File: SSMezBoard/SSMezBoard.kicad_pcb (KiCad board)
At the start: 2 copper layers, 2 parts, among them U1 DFRobot_DC_Controller

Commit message: Sort of ready for JLCPCB
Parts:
- removed U1: DFRobot_DC_Controller, PBFootPrintLibrary:DFRobot_DC_Controller
- added J1: Conn_02x10_Odd_Even, Connector_PinHeader_2.54mm:PinHeader_2x10_P2.54mm_Horizontal, F.Cu at (162.9, 75.8)
- added LED1: LED, LED_THT:LED_D5.0mm, F.Cu at (160.1, 108.5)
- added LED2: LED, LED_THT:LED_D5.0mm, F.Cu at (166.1, 64.4)
- added SW1: TACT_SW, Button_Switch_THT:SW_PUSH_6mm, F.Cu at (144.2, 112.7)
- moved A1 40.3 mm to (157.6, 97.6), turned to 180 degrees
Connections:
- net Net-(A1-GND-Pad29) renamed GND
- A1 pad 1: unconnected-(A1-D1/TX-Pad1) -> Net-(A1-D1/TX)
- A1 pad 10: unconnected-(A1-D7-Pad10) -> RIGHT_ENC_B
- A1 pad 11: unconnected-(A1-D8-Pad11) -> LEFT_ENC_A
- A1 pad 12: unconnected-(A1-D9-Pad12) -> LEFT_ENC_B
- A1 pad 13: unconnected-(A1-D10/CS-Pad13) -> SENSOR_LED
- A1 pad 14: unconnected-(A1-D11/COPI-Pad14) -> GPIO_DIAG
- A1 pad 15: unconnected-(A1-D12/CIPO-Pad15) -> GPIO_FRONT
- A1 pad 16: unconnected-(A1-D13/SCK-Pad16) -> Net-(A1-D13/SCK)
- A1 pad 17: Net-(A1-3V3) -> Vcc
- A1 pad 19: unconnected-(A1-A0-Pad19) -> RIGHT_DIAG_ADC
- A1 pad 2: unconnected-(A1-D0/RX-Pad2) -> Net-(A1-D0/RX)
- A1 pad 20: unconnected-(A1-A1-Pad20) -> RIGHT_FRONT_ADC
- A1 pad 21: unconnected-(A1-A2-Pad21) -> LEFT_FRONT_ADC
- A1 pad 22: unconnected-(A1-A3-Pad22) -> LEFT_DIAG_ADC
- A1 pad 23: unconnected-(A1-SDA/A4-Pad23) -> GPIO12_D18
- A1 pad 30: unconnected-(A1-VIN-Pad30) -> Vbatt
- A1 pad 5: unconnected-(A1-D2-Pad5) -> RIGHT_Motor_PWM
- A1 pad 6: unconnected-(A1-D3-Pad6) -> LEFT_Motor_PWM
- A1 pad 7: unconnected-(A1-D4-Pad7) -> LEFT_Motor_Dir
- A1 pad 8: unconnected-(A1-D5-Pad8) -> RIGHT_Motor_Dir
- A1 pad 9: unconnected-(A1-D6-Pad9) -> RIGHT_ENC_A
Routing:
- net RIGHT_DIAG_ADC: track 0.00 -> 38.3 mm, vias 0 -> 1
- net Vcc: track 0.00 -> 37.5 mm
- net LEFT_FRONT_ADC: track 0.00 -> 34.8 mm
- net GPIO12_D18: track 0.00 -> 33.8 mm
- net RIGHT_FRONT_ADC: track 0.00 -> 31.0 mm, vias 0 -> 1
- net LEFT_DIAG_ADC: track 0.00 -> 29.0 mm
- net Net-(A1-D13/SCK): track 0.00 -> 26.2 mm
- net GPIO_FRONT: track 0.00 -> 22.8 mm
- net GPIO_DIAG: track 0.00 -> 22.7 mm
- net Vbatt: track 0.00 -> 22.7 mm
- net Net-(A1-D1/TX): track 0.00 -> 18.9 mm
- net SENSOR_LED: track 0.00 -> 15.3 mm
- net Net-(A1-D0/RX): track 0.00 -> 13.1 mm
- net LEFT_Motor_PWM: track 0.00 -> 9.32 mm
- net RIGHT_Motor_Dir: track 0.00 -> 9.16 mm
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- added copper zone on B.Cu, net GND
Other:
- board outline added: 30 x 60 mm
- board text added: "${designer}"
- board text added: "Ardunio Nano Connect RP2040"
- board text added: "Version ${version}"

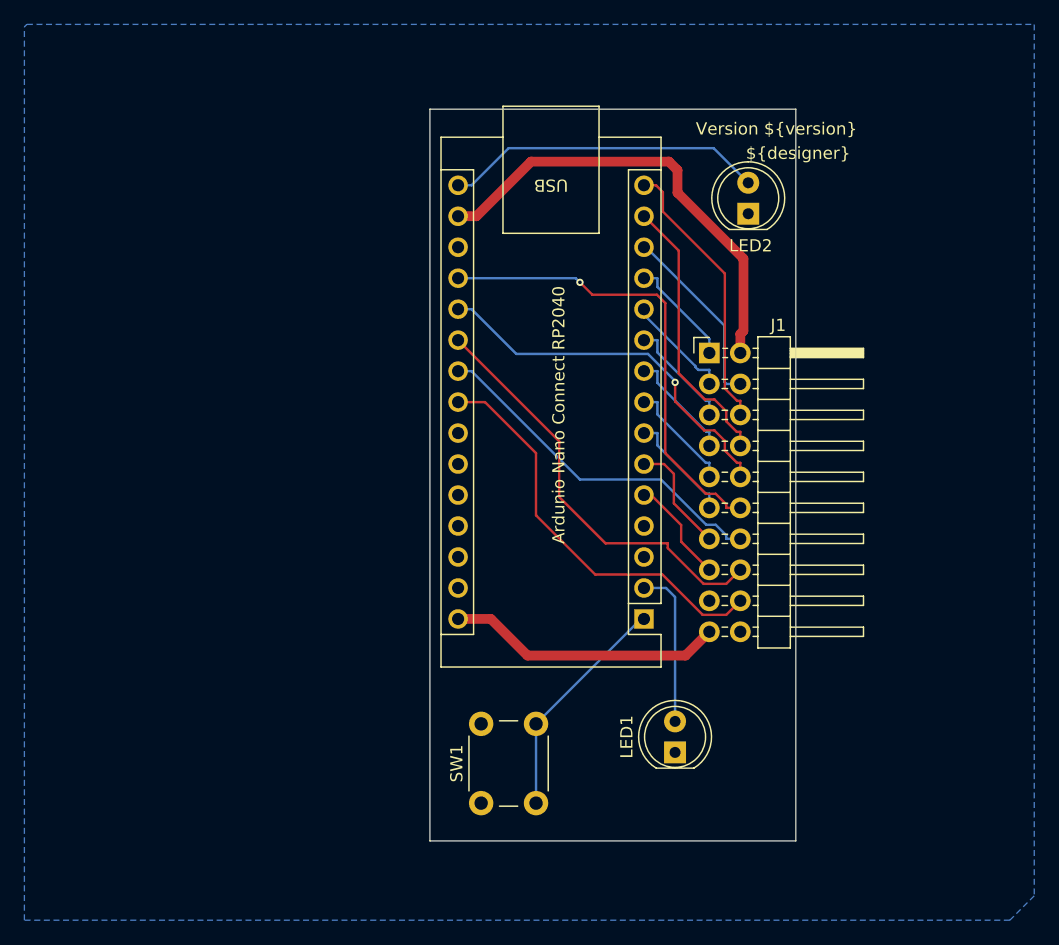
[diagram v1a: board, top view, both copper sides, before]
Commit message: Version 2 of boards sent to JLCPCB and a new calibration board
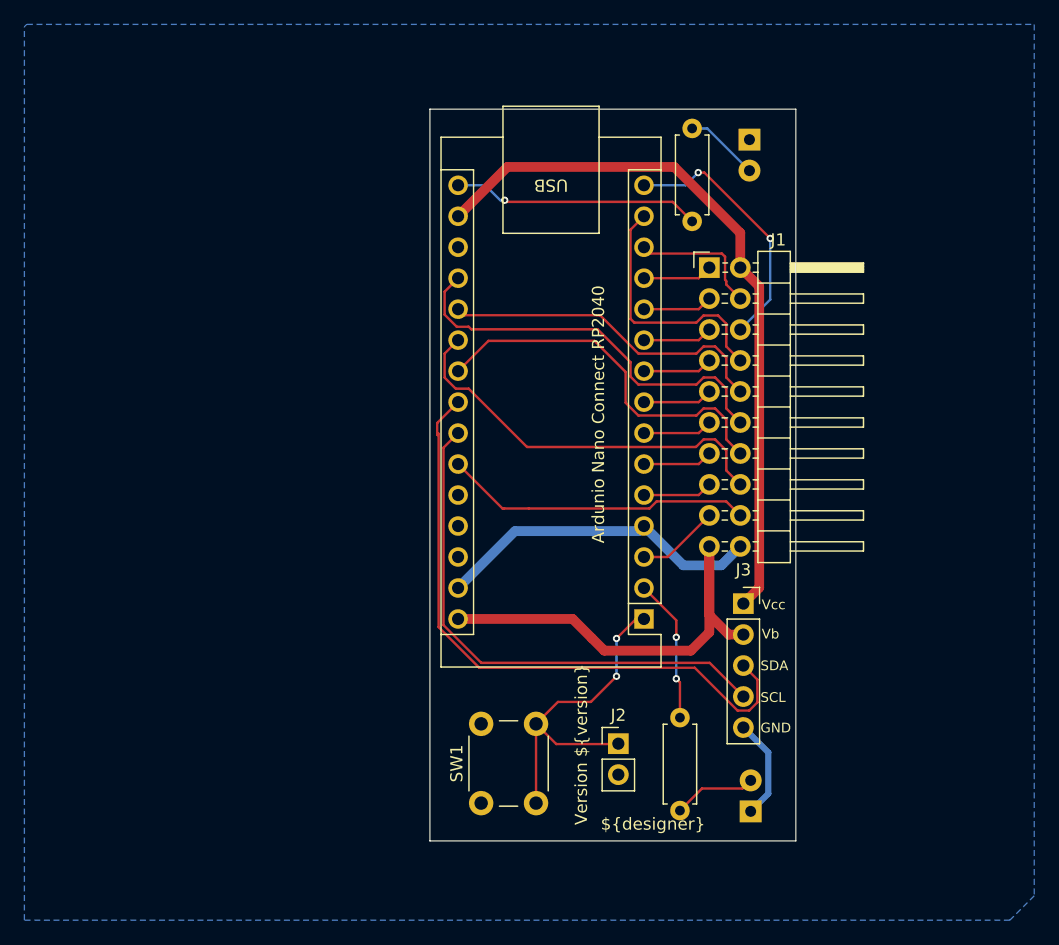
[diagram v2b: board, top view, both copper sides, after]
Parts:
- added J2: Conn_01x02, Connector_PinHeader_2.54mm:PinHeader_1x02_P2.54mm_Vertical, F.Cu at (155.4, 107.8)
- added J3: Conn_01x05, Connector_PinSocket_2.54mm:PinSocket_1x05_P2.54mm_Vertical, F.Cu at (165.7, 96.3)
- added R1: 1K, Resistor_THT:R_Axial_DIN0207_L6.3mm_D2.5mm_P7.62mm_Horizontal, F.Cu at (161.5, 57.4)
- added R2: 1K, Resistor_THT:R_Axial_DIN0207_L6.3mm_D2.5mm_P7.62mm_Horizontal, F.Cu at (160.5, 105.7)
- D1: renamed from LED1; moved to B.Cu
- D2: renamed from LED2; moved to B.Cu
- moved D1 7.86 mm to (166.3, 113.4)
- moved J1 7.00 mm to (162.9, 68.8)
- moved D2 6.08 mm to (166.2, 58.3), turned to -90 degrees
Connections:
- A1 pad 23: GPIO12_D18 -> Net-(A1-SDA/A4)
- A1 pad 24: unconnected-(A1-SCL/A5-Pad24) -> Net-(A1-SCL/A5)
- A1 pad 25: unconnected-(A1-A6-Pad25) -> D18_A6
- A1 pad 3: unconnected-(A1-~{RESET}-Pad3) -> RESET
- D1 pad 2: Net-(A1-D0/RX) -> Net-(D1-A)
- D2 pad 2: Net-(A1-D13/SCK) -> Net-(D2-A)
- J1 pad 17: unconnected-(J1-Pin_17-Pad17) -> RESET
- J1 pad 18: GPIO12_D18 -> D18_A6
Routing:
- net Net-(A1-SDA/A4): track 0.00 -> 52.2 mm
- net Net-(A1-SCL/A5): track 0.00 -> 43.3 mm
- net GND: track 0.00 -> 35.5 mm
- net GPIO12_D18: track 33.8 -> 0.00 mm
- net D18_A6: track 0.00 -> 25.4 mm
- net Vcc: track 37.5 -> 58.6 mm
- net Vbatt: track 22.7 -> 38.4 mm
- net Net-(A1-D1/TX): track 18.9 -> 27.8 mm, vias 0 -> 2
- net Net-(D1-A): track 0.00 -> 6.83 mm
- net RESET: track 0.00 -> 6.77 mm
- net Net-(D2-A): track 0.00 -> 6.13 mm
- net Net-(A1-D13/SCK): track 26.2 -> 20.4 mm, vias 0 -> 1
- net RIGHT_DIAG_ADC: track 38.3 -> 33.5 mm, vias 1 -> 0
- net SENSOR_LED: track 15.3 -> 10.9 mm
- net LEFT_Motor_PWM: track 9.32 -> 5.72 mm
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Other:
- board text added: "GND"
- board text added: "SCL"
- board text added: "SDA"
- board text added: "Vb"
- board text added: "Vcc"
